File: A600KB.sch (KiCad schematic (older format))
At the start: 78 parts

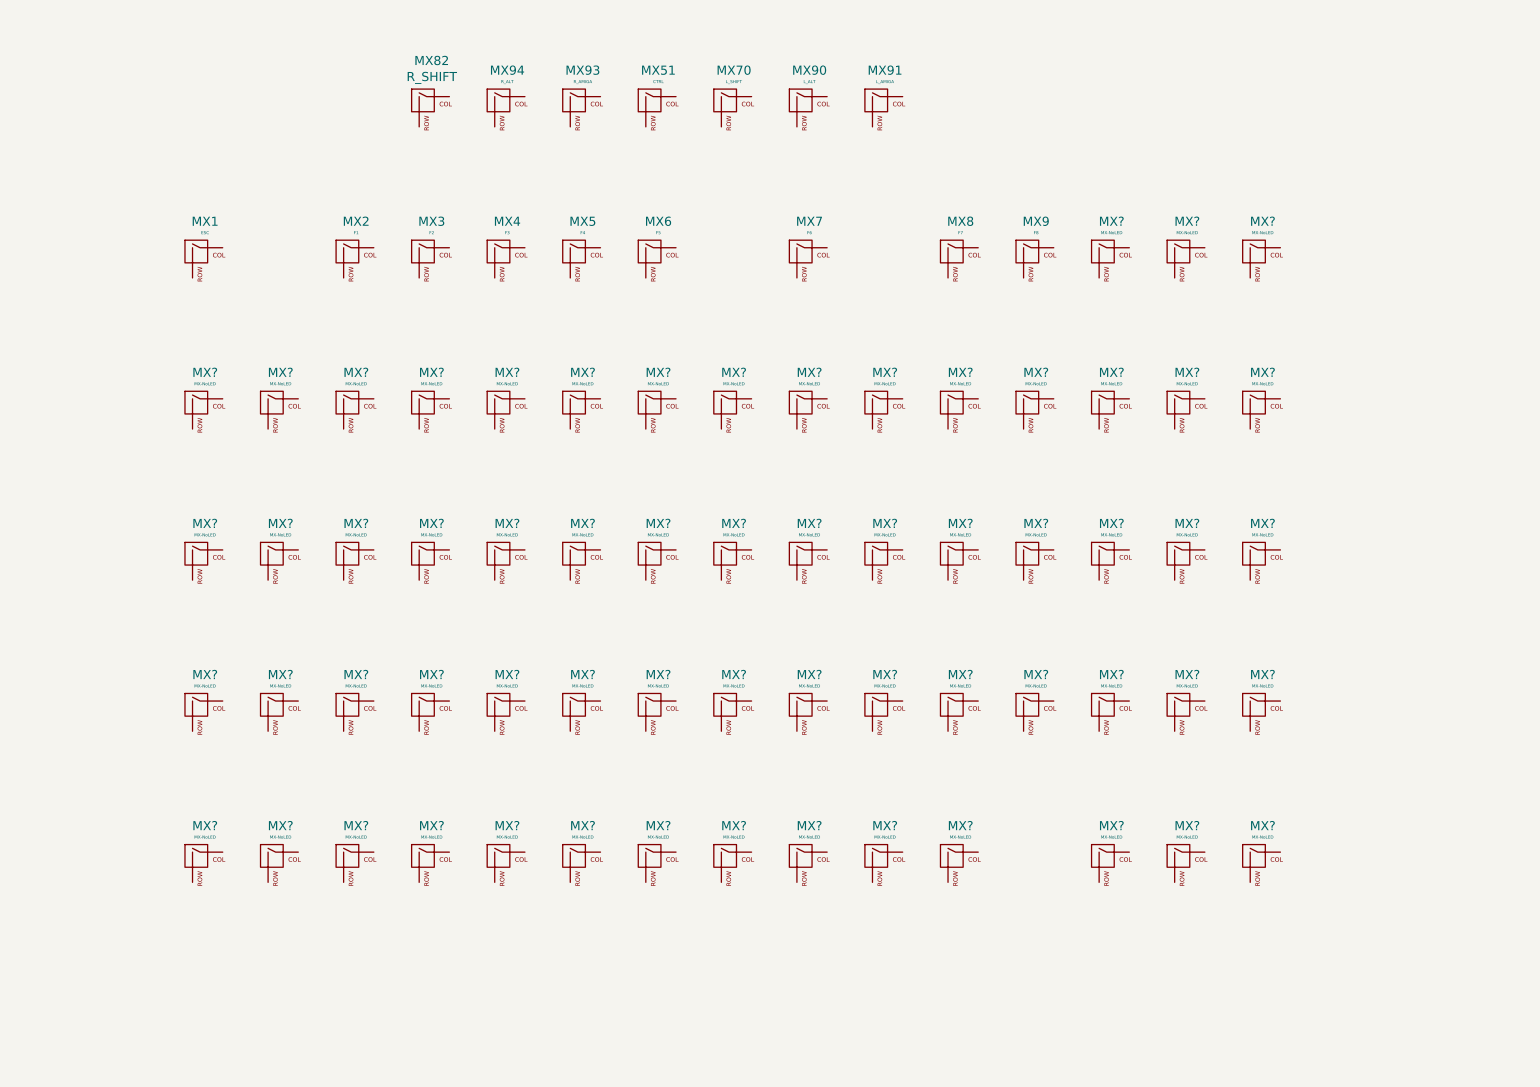
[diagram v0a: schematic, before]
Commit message: Schematic without connectors
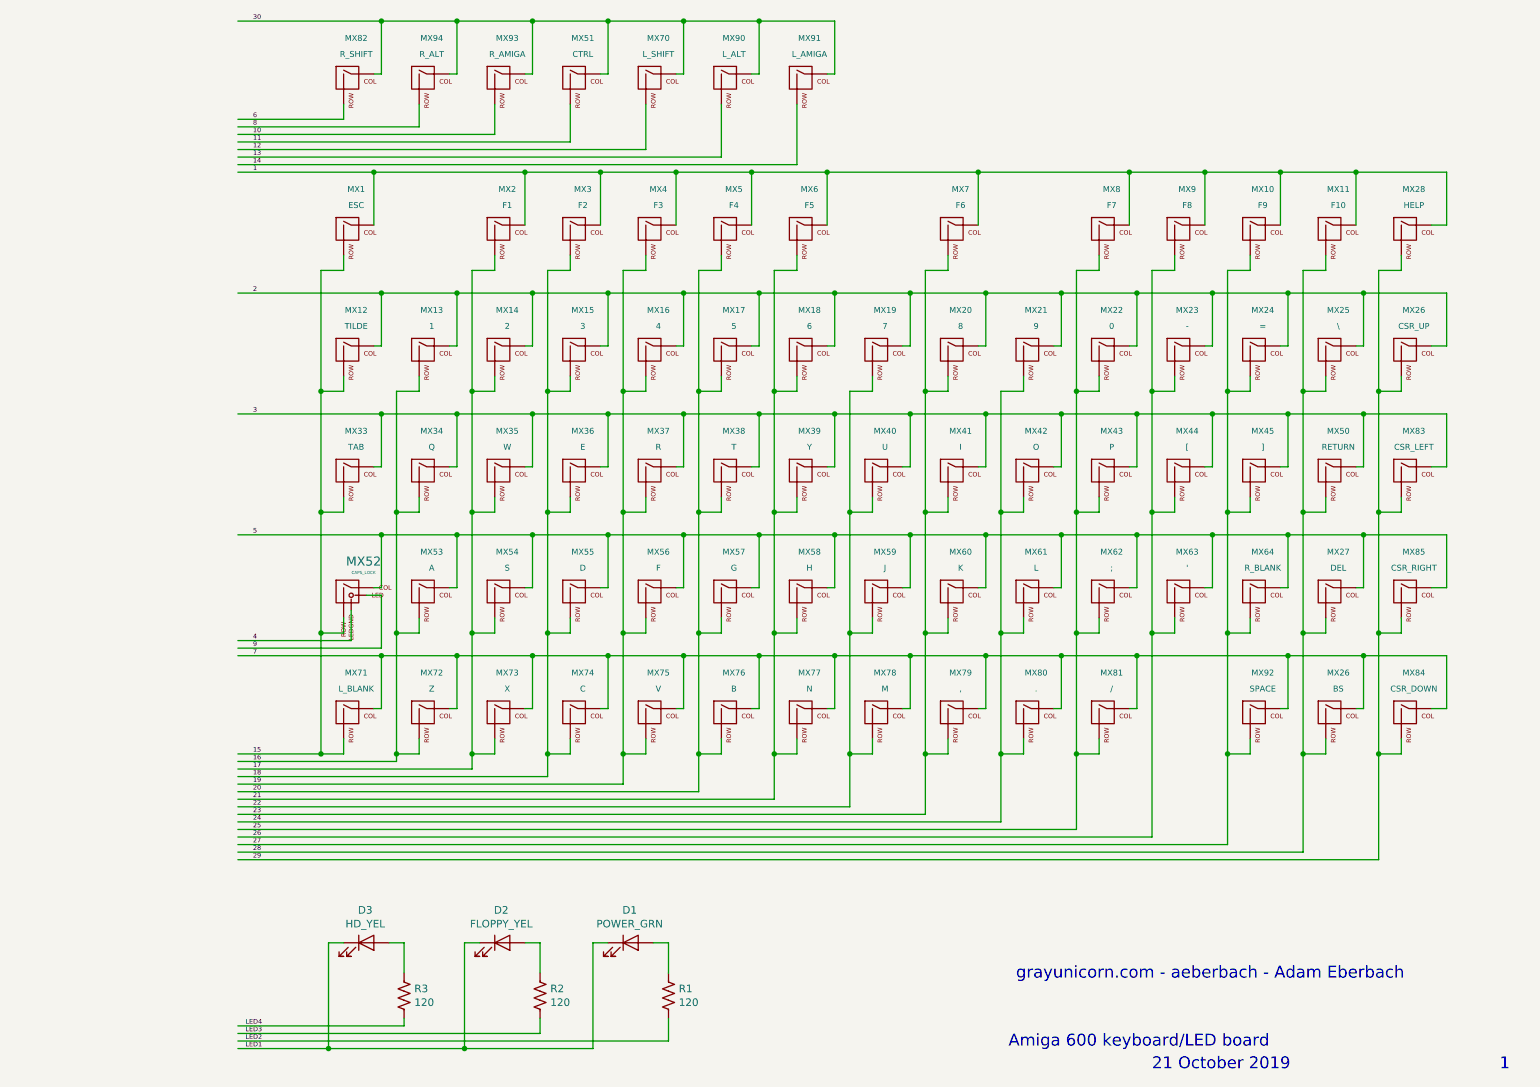
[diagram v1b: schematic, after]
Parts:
- removed MX? (x62): MX-NoLED, symbol MX_Alps_Hybrid:MX-NoLED
- added D1: POWER_GRN, symbol Device:LED
- added D2: FLOPPY_YEL, symbol Device:LED
- added D3: HD_YEL, symbol Device:LED
- added MX10: F9, MX_Only:MXOnly-1.25U-NoLED, symbol MX_Alps_Hybrid:MX-NoLED
- added MX11: F10, MX_Only:MXOnly-1.25U-NoLED, symbol MX_Alps_Hybrid:MX-NoLED
- added MX12: TILDE, MX_Only:MXOnly-1.5U-NoLED, symbol MX_Alps_Hybrid:MX-NoLED
- added MX13: 1, MX_Only:MXOnly-1U-NoLED, symbol MX_Alps_Hybrid:MX-NoLED
- added MX14: 2, MX_Only:MXOnly-1U-NoLED, symbol MX_Alps_Hybrid:MX-NoLED
- added MX15: 3, MX_Only:MXOnly-1U-NoLED, symbol MX_Alps_Hybrid:MX-NoLED
- added MX16: 4, MX_Only:MXOnly-1U-NoLED, symbol MX_Alps_Hybrid:MX-NoLED
- added MX17: 5, MX_Only:MXOnly-1U-NoLED, symbol MX_Alps_Hybrid:MX-NoLED
- added MX18: 6, MX_Only:MXOnly-1U-NoLED, symbol MX_Alps_Hybrid:MX-NoLED
- added MX19: 7, MX_Only:MXOnly-1U-NoLED, symbol MX_Alps_Hybrid:MX-NoLED
- added MX20: 8, MX_Only:MXOnly-1U-NoLED, symbol MX_Alps_Hybrid:MX-NoLED
- added MX21: 9, MX_Only:MXOnly-1U-NoLED, symbol MX_Alps_Hybrid:MX-NoLED
- added MX22: 0, MX_Only:MXOnly-1U-NoLED, symbol MX_Alps_Hybrid:MX-NoLED
- added MX23: -, MX_Only:MXOnly-1U-NoLED, symbol MX_Alps_Hybrid:MX-NoLED
- added MX24: =, MX_Only:MXOnly-1U-NoLED, symbol MX_Alps_Hybrid:MX-NoLED
- added MX25: \\, MX_Only:MXOnly-1U-NoLED, symbol MX_Alps_Hybrid:MX-NoLED
- added MX26: CSR_UP, MX_Only:MXOnly-1U-NoLED, symbol MX_Alps_Hybrid:MX-NoLED
- added MX26: BS, MX_Only:MXOnly-1U-NoLED, symbol MX_Alps_Hybrid:MX-NoLED
- added MX27: DEL, MX_Only:MXOnly-1U-NoLED, symbol MX_Alps_Hybrid:MX-NoLED
- added MX28: HELP, MX_Only:MXOnly-1.25U-NoLED, symbol MX_Alps_Hybrid:MX-NoLED
- added MX33: TAB, MX_Only:MXOnly-2.25U-NoLED, symbol MX_Alps_Hybrid:MX-NoLED
- added MX34: Q, MX_Only:MXOnly-1U-NoLED, symbol MX_Alps_Hybrid:MX-NoLED
- added MX35: W, MX_Only:MXOnly-1U-NoLED, symbol MX_Alps_Hybrid:MX-NoLED
- added MX36: E, MX_Only:MXOnly-1U-NoLED, symbol MX_Alps_Hybrid:MX-NoLED
- added MX37: R, MX_Only:MXOnly-1U-NoLED, symbol MX_Alps_Hybrid:MX-NoLED
- added MX38: T, MX_Only:MXOnly-1U-NoLED, symbol MX_Alps_Hybrid:MX-NoLED
- added MX39: Y, MX_Only:MXOnly-1U-NoLED, symbol MX_Alps_Hybrid:MX-NoLED
- added MX40: U, MX_Only:MXOnly-1U-NoLED, symbol MX_Alps_Hybrid:MX-NoLED
- added MX41: I, MX_Only:MXOnly-1U-NoLED, symbol MX_Alps_Hybrid:MX-NoLED
- added MX42: O, MX_Only:MXOnly-1U-NoLED, symbol MX_Alps_Hybrid:MX-NoLED
- added MX43: P, MX_Only:MXOnly-1U-NoLED, symbol MX_Alps_Hybrid:MX-NoLED
- added MX44: [, MX_Only:MXOnly-1U-NoLED, symbol MX_Alps_Hybrid:MX-NoLED
- added MX45: ], MX_Only:MXOnly-1U-NoLED, symbol MX_Alps_Hybrid:MX-NoLED
- added MX50: RETURN, MX_Only:MXOnly-ISO, symbol MX_Alps_Hybrid:MX-NoLED
- added MX52: CAPS_LOCK, MX_Only:MXOnly-1U, symbol MX_Alps_Hybrid:MX-LED
- added MX53: A, MX_Only:MXOnly-1U-NoLED, symbol MX_Alps_Hybrid:MX-NoLED
- added MX54: S, MX_Only:MXOnly-1U-NoLED, symbol MX_Alps_Hybrid:MX-NoLED
- added MX55: D, MX_Only:MXOnly-1U-NoLED, symbol MX_Alps_Hybrid:MX-NoLED
- added MX56: F, MX_Only:MXOnly-1U-NoLED, symbol MX_Alps_Hybrid:MX-NoLED
- added MX57: G, MX_Only:MXOnly-1U-NoLED, symbol MX_Alps_Hybrid:MX-NoLED
- added MX58: H, MX_Only:MXOnly-1U-NoLED, symbol MX_Alps_Hybrid:MX-NoLED
- added MX59: J, MX_Only:MXOnly-1U-NoLED, symbol MX_Alps_Hybrid:MX-NoLED
- added MX60: K, MX_Only:MXOnly-1U-NoLED, symbol MX_Alps_Hybrid:MX-NoLED
- added MX61: L, MX_Only:MXOnly-1U-NoLED, symbol MX_Alps_Hybrid:MX-NoLED
- added MX62: ;, MX_Only:MXOnly-1U-NoLED, symbol MX_Alps_Hybrid:MX-NoLED
- added MX63: ', MX_Only:MXOnly-1U-NoLED, symbol MX_Alps_Hybrid:MX-NoLED
- added MX64: R_BLANK, MX_Only:MXOnly-1U-NoLED, symbol MX_Alps_Hybrid:MX-NoLED
- added MX71: L_BLANK, MX_Only:MXOnly-1U-NoLED, symbol MX_Alps_Hybrid:MX-NoLED
- added MX72: Z, MX_Only:MXOnly-1U-NoLED, symbol MX_Alps_Hybrid:MX-NoLED
- added MX73: X, MX_Only:MXOnly-1U-NoLED, symbol MX_Alps_Hybrid:MX-NoLED
- added MX74: C, MX_Only:MXOnly-1U-NoLED, symbol MX_Alps_Hybrid:MX-NoLED
- added MX75: V, MX_Only:MXOnly-1U-NoLED, symbol MX_Alps_Hybrid:MX-NoLED
- added MX76: B, MX_Only:MXOnly-1U-NoLED, symbol MX_Alps_Hybrid:MX-NoLED
- added MX77: N, MX_Only:MXOnly-1U-NoLED, symbol MX_Alps_Hybrid:MX-NoLED
- added MX78: M, MX_Only:MXOnly-1U-NoLED, symbol MX_Alps_Hybrid:MX-NoLED
- added MX79: ,, MX_Only:MXOnly-1U-NoLED, symbol MX_Alps_Hybrid:MX-NoLED
- added MX80: ., MX_Only:MXOnly-1U-NoLED, symbol MX_Alps_Hybrid:MX-NoLED
- added MX81: /, MX_Only:MXOnly-1U-NoLED, symbol MX_Alps_Hybrid:MX-NoLED
- added MX83: CSR_LEFT, MX_Only:MXOnly-1U-NoLED, symbol MX_Alps_Hybrid:MX-NoLED
- added MX84: CSR_DOWN, MX_Only:MXOnly-1U-NoLED, symbol MX_Alps_Hybrid:MX-NoLED
- added MX85: CSR_RIGHT, MX_Only:MXOnly-1U-NoLED, symbol MX_Alps_Hybrid:MX-NoLED
- added MX92: SPACE, MX_Only:MXOnly-7U, symbol MX_Alps_Hybrid:MX-NoLED
- added R1, R2, R3: 120, symbol Device:R_US
- MX1, MX2, MX3, MX4, MX5, MX51, MX6, MX7, MX8, MX9, MX90, MX91, MX93: footprint (none) -> MX_Only:MXOnly-1.25U-NoLED
- MX70, MX82: footprint (none) -> MX_Only:MXOnly-2U-NoLED
- MX94: footprint (none) -> MX_Only:MXOnly-1U-NoLED
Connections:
- net labels added: 1, 10, 11, 12, 13, 14, 15, 16, 17, 18, 19, 2, 20, 21, 22, 23, 24, 25, 26, 27, 28, 29, 3, 30, 4, 5, 6, 7, 8, 9, LED1, LED2, LED3, LED4
- wire segments 0 -> 490
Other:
- note added: "1"
- note added: "21 October 2019"
- note added: "Amiga 600 keyboard/LED board"
- note added: "grayunicorn.com - aeberbach - Adam Eberbach"
- moved on the sheet: MX82
